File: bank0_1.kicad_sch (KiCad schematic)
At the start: 1 part, among them U1 ECP5-BGA256

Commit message: schematic wip
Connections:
- net +3V3: no longer U1.D10 (PT47A), U1.E10 (PT47B), U1.E11 (PT51B), U1.F10 (VCCIO1_1), U1.F11 (VCCIO1_2)
- net RX_MIX_CTRL.FM: now reaches U1.A2 (PT4A)
- net RX_MIX_CTRL.ENBL: now reaches U1.A3 (PT6A)
- net RX_MIX_CTRL.MODE: now reaches U1.A4 (PT6B)
- net RX_MIX_CTRL.LD: now reaches U1.B3 (PT4B)
- net RX_MIX_CTRL.SCLK: now reaches U1.C4 (PT11A)
- net RX_RCVR.SDA: now reaches U1.C6 (PT22A)
- net ~{RX_MIX_BYPASS}: now reaches U1.C7 (PT27A)
- net RX_MIX_CTRL.~{EN}: now reaches U1.D4 (PT9B)
- net RX_RCVR.GAIN5: now reaches U1.D5 (PT13B)
- net RX_RCVR.GAIN0: now reaches U1.D6 (PT20B)
- net 3V3RX_EN: now reaches U1.D7 (PT24B)
- net RX_MIX_CTRL.~{RESET}: now reaches U1.E4 (PT9A)
- net CLOCK_60MHZ: no longer names the net of U1.A8 (PT29B)
- net LED0: no longer names the net of U1.E13 (PT62B)
- net LED1 renamed AFE_SPI.SCK
- net LED2: no longer names the net of U1.B14 (PT67A)
- net LED3 renamed AFE_ALT_CLK
- net LED4 renamed DA0
- net LED5 renamed DA6
- net MEZZANINE22: no longer names the net of U1.A14 (PT65B)
- net MEZZANINE23 renamed AFE_SPI.PICO
- net MEZZANINE24: no longer names the net of U1.A13 (PT65A)
- net MEZZANINE25 renamed AFE_SPI.~{CS}
- net MEZZANINE26 renamed DA3
- net MEZZANINE27 renamed DA2
- net MEZZANINE28 renamed DA4
- net MEZZANINE3 renamed DD7
- net MEZZANINE4 renamed DD3
- net MEZZANINE5 renamed DD1
- net MEZZANINE6 renamed DD2
- net MEZZANINE7 renamed DA7
- net PMOD_A0 renamed DD5
- net PMOD_A1 renamed DD6
- net PMOD_A2 renamed DA5
- net PMOD_A3 renamed DA1
- net PMOD_A4 renamed DD8
- net PMOD_A5 renamed DD9
- net PMOD_A6 renamed DD4
- net PMOD_A7 renamed DD0
- net PMOD_B0 renamed RX_MIX_CTRL.SDATA
- net PMOD_B1 renamed RX_RCVR.GAIN3
- net PMOD_B2 renamed RX_RCVR.SCL
- net PMOD_B3: no longer names the net of U1.B7 (PT27B)
- net PMOD_B4 renamed RX_RCVR.GAIN4
- net PMOD_B5 renamed RX_RCVR.GAIN2
- net PMOD_B6 renamed RX_RCVR.GAIN1
- net PMOD_B7: no longer names the net of U1.A7 (PT29A)
- new net +1V8: U1.D10 (PT47A), U1.E10 (PT47B), U1.E11 (PT51B), U1.F10 (VCCIO1_1), U1.F11 (VCCIO1_2)
- no-connect marks 12 -> 7
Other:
- moved on the sheet: U1B, U1C

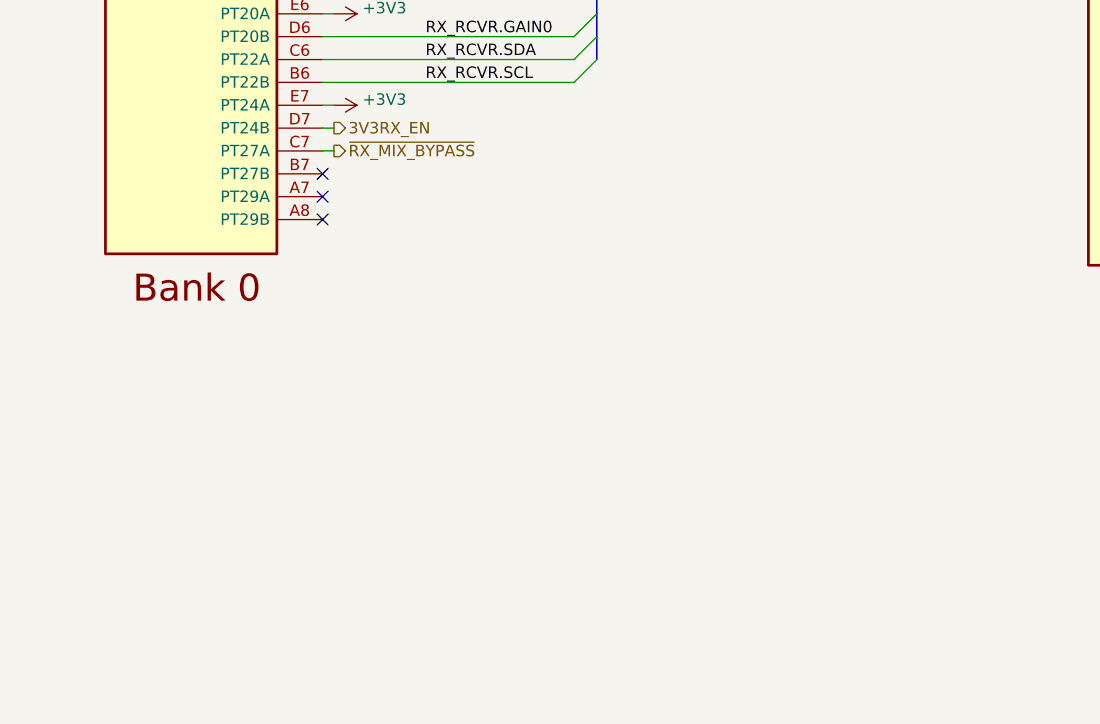
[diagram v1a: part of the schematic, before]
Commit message: add regulator for analog 3.3 V supply
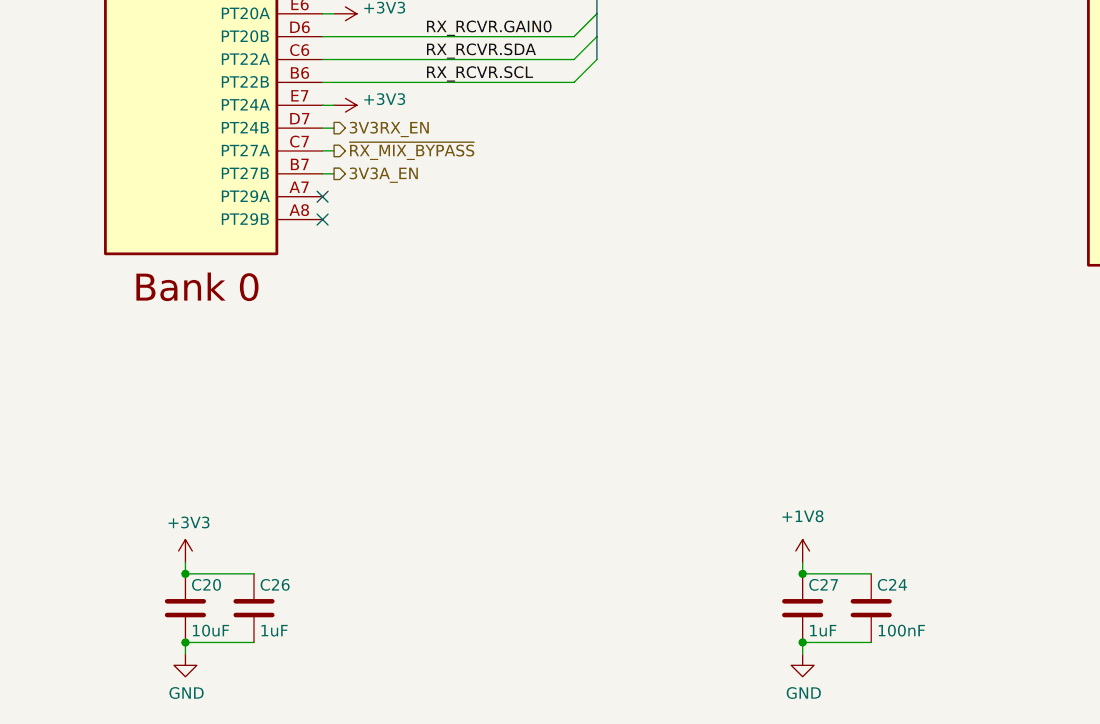
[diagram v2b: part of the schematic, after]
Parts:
- added C20: 10uF, Capacitor_SMD:C_0603_1608Metric, symbol Device:C
- added C24: 100nF, Capacitor_SMD:C_0402_1005Metric, symbol Device:C
- added C26, C27: 1uF, Capacitor_SMD:C_0402_1005Metric, symbol Device:C
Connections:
- net +1V8: now also C24.1, C27.1
- net +3V3: now also C20.1, C26.1
- net GND: now also C20.2, C24.2, C26.2, C27.2
- net 3V3A_EN: now reaches U1.B7 (PT27B)
- no-connect marks 7 -> 6

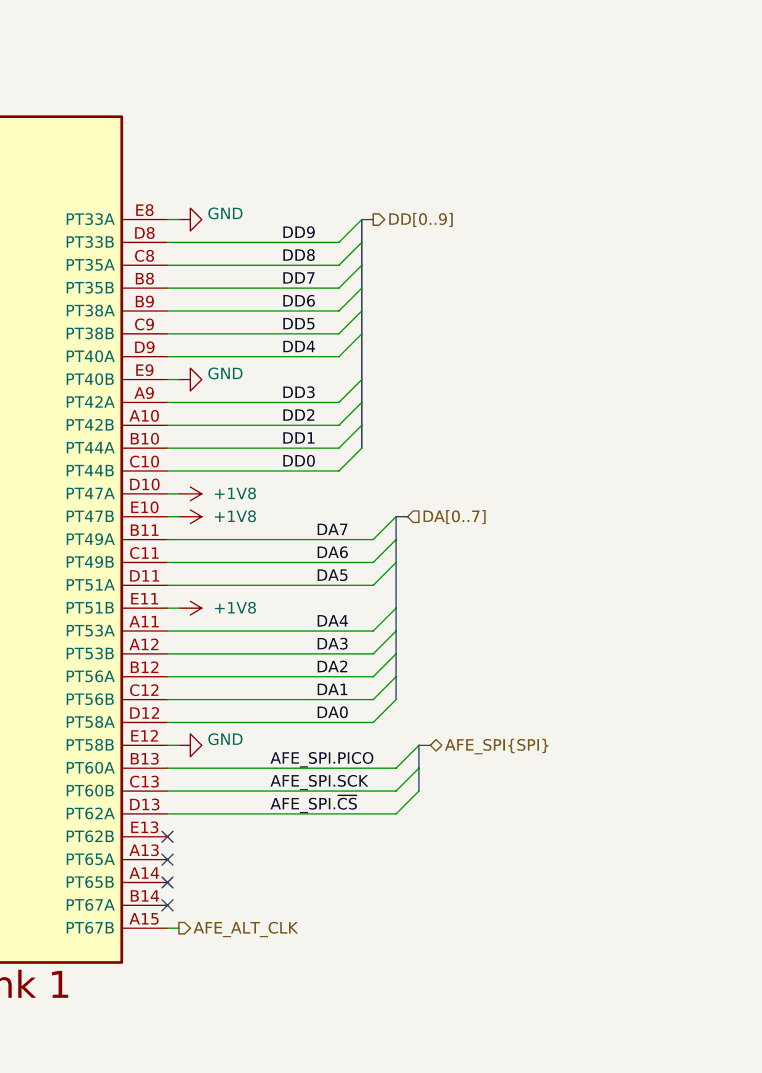
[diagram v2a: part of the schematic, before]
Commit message: ADC/DAC layout
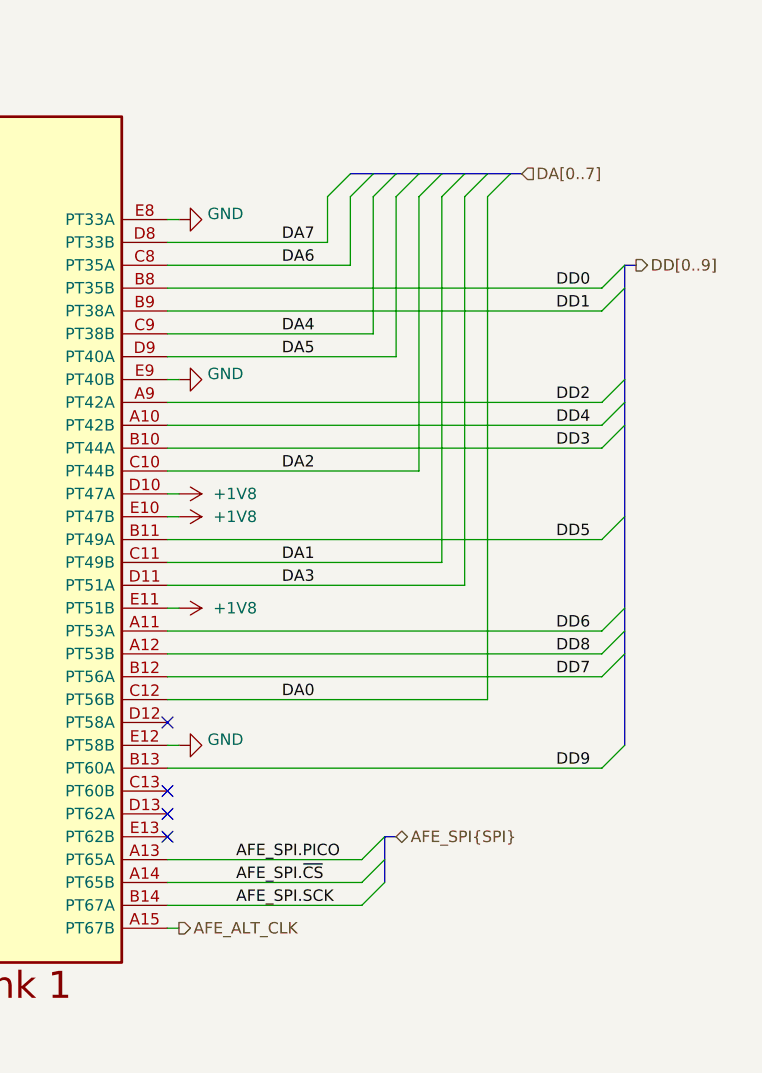
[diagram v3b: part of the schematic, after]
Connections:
- net AFE_SPI.PICO: now also U1.A13 (PT65A); no longer U1.B13 (PT60A)
- net AFE_SPI.SCK: now also U1.B14 (PT67A); no longer U1.C13 (PT60B)
- net AFE_SPI.~{CS}: now also U1.A14 (PT65B); no longer U1.D13 (PT62A)
- net DA0: now also U1.C12 (PT56B); no longer U1.D12 (PT58A)
- net DA1: now also U1.C11 (PT49B); no longer U1.C12 (PT56B)
- net DA2: now also U1.C10 (PT44B); no longer U1.B12 (PT56A)
- net DA3: now also U1.D11 (PT51A); no longer U1.A12 (PT53B)
- net DA4: now also U1.C9 (PT38B); no longer U1.A11 (PT53A)
- net DA5: now also U1.D9 (PT40A); no longer U1.D11 (PT51A)
- net DA6: now also U1.C8 (PT35A); no longer U1.C11 (PT49B)
- net DA7: now also U1.D8 (PT33B); no longer U1.B11 (PT49A)
- net DD0: now also U1.B8 (PT35B); no longer U1.C10 (PT44B)
- net DD1: now also U1.B9 (PT38A); no longer U1.B10 (PT44A)
- net DD2: now also U1.A9 (PT42A); no longer U1.A10 (PT42B)
- net DD3: now also U1.B10 (PT44A); no longer U1.A9 (PT42A)
- net DD4: now also U1.A10 (PT42B); no longer U1.D9 (PT40A)
- net DD5: now also U1.B11 (PT49A); no longer U1.C9 (PT38B)
- net DD6: now also U1.A11 (PT53A); no longer U1.B9 (PT38A)
- net DD7: now also U1.B12 (PT56A); no longer U1.B8 (PT35B)
- net DD8: now also U1.A12 (PT53B); no longer U1.C8 (PT35A)
- net DD9: now also U1.B13 (PT60A); no longer U1.D8 (PT33B)

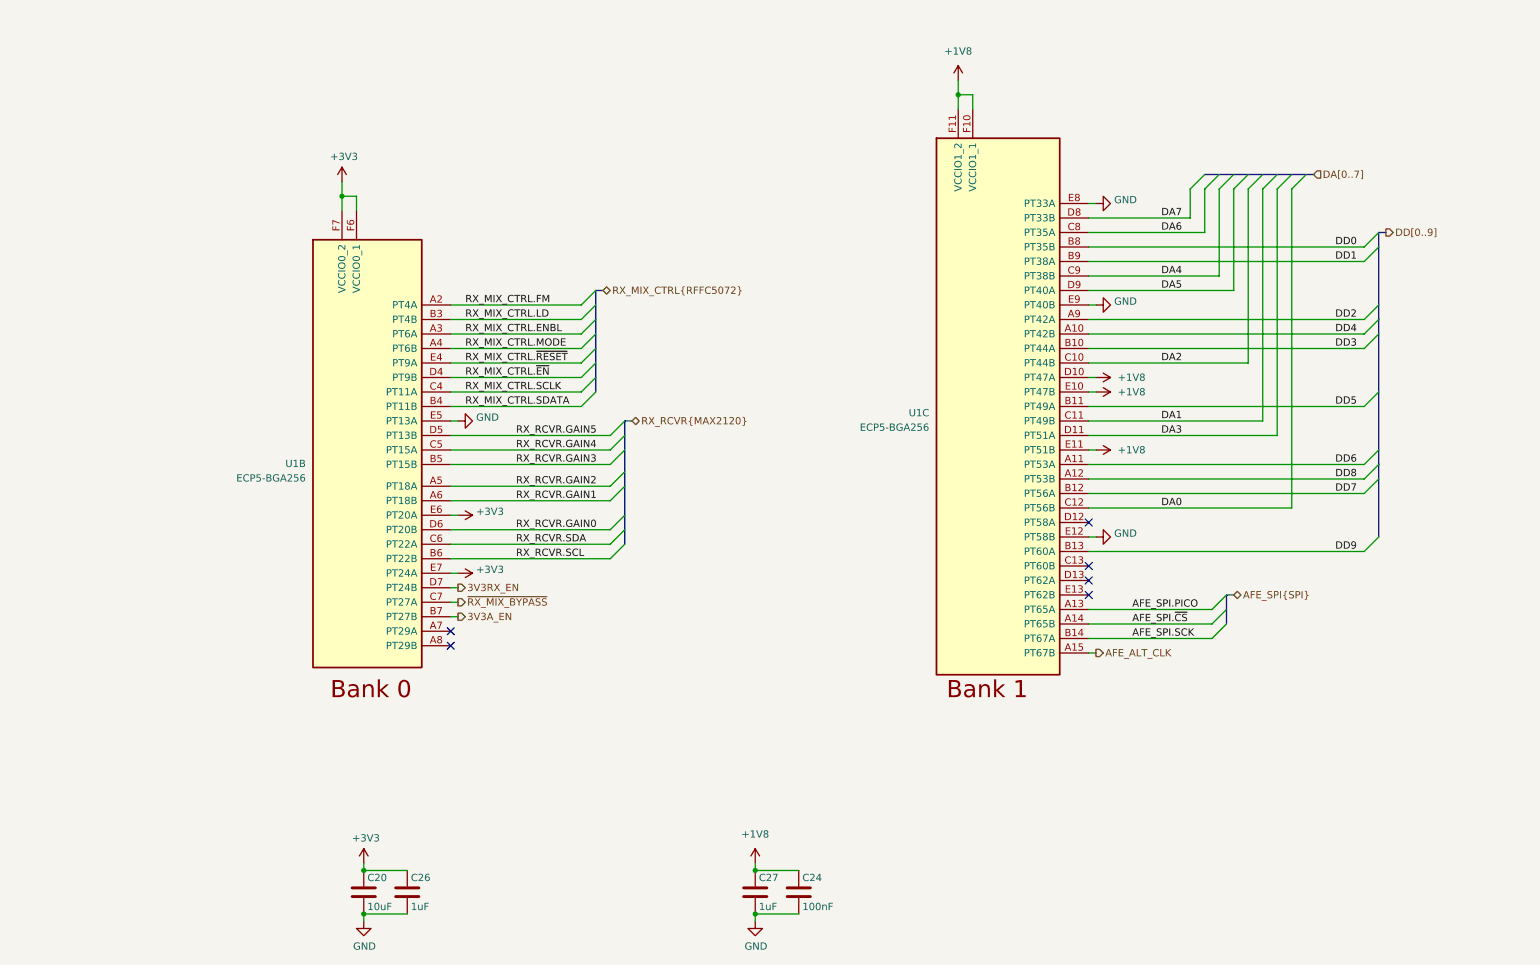
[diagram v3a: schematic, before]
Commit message: layout wip: radio FPGA connections and clocks
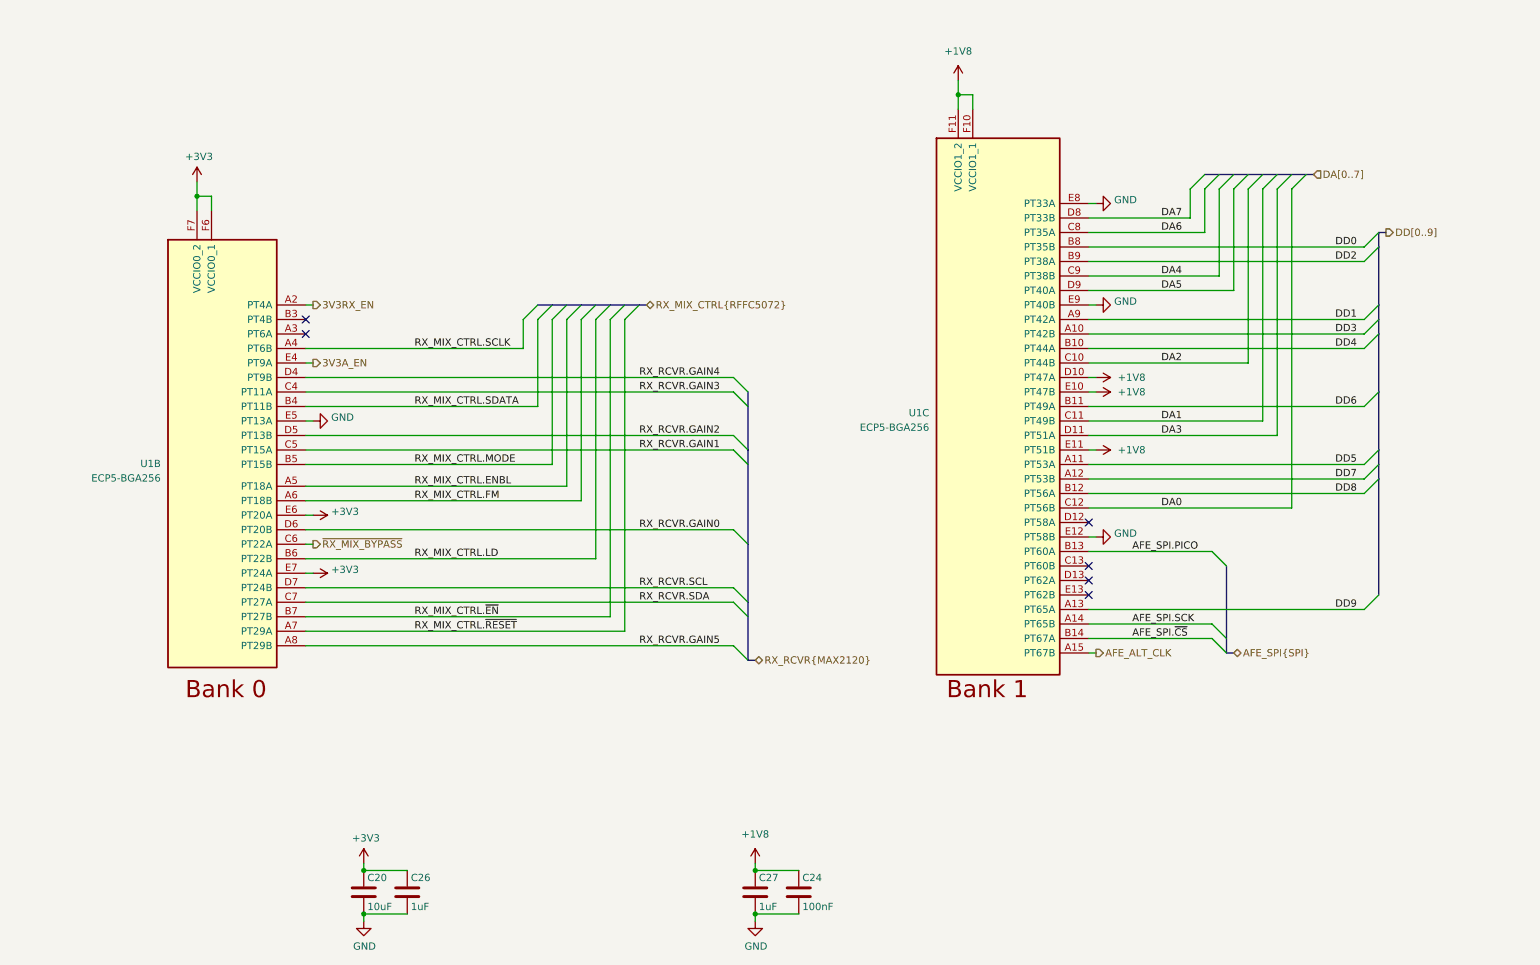
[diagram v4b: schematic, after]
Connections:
- net 3V3A_EN: now also U1.E4 (PT9A); no longer U1.B7 (PT27B)
- net 3V3RX_EN: now also U1.A2 (PT4A); no longer U1.D7 (PT24B)
- net AFE_SPI.PICO: now also U1.B13 (PT60A); no longer U1.A13 (PT65A)
- net AFE_SPI.SCK: now also U1.A14 (PT65B); no longer U1.B14 (PT67A)
- net AFE_SPI.~{CS}: now also U1.B14 (PT67A); no longer U1.A14 (PT65B)
- net DD1: now also U1.A9 (PT42A); no longer U1.B9 (PT38A)
- net DD2: now also U1.B9 (PT38A); no longer U1.A9 (PT42A)
- net DD3: now also U1.A10 (PT42B); no longer U1.B10 (PT44A)
- net DD4: now also U1.B10 (PT44A); no longer U1.A10 (PT42B)
- net DD5: now also U1.A11 (PT53A); no longer U1.B11 (PT49A)
- net DD6: now also U1.B11 (PT49A); no longer U1.A11 (PT53A)
- net DD7: now also U1.A12 (PT53B); no longer U1.B12 (PT56A)
- net DD8: now also U1.B12 (PT56A); no longer U1.A12 (PT53B)
- net DD9: now also U1.A13 (PT65A); no longer U1.B13 (PT60A)
- net RX_MIX_CTRL.ENBL: now also U1.A5 (PT18A); no longer U1.A3 (PT6A)
- net RX_MIX_CTRL.FM: now also U1.A6 (PT18B); no longer U1.A2 (PT4A)
- net RX_MIX_CTRL.LD: now also U1.B6 (PT22B); no longer U1.B3 (PT4B)
- net RX_MIX_CTRL.MODE: now also U1.B5 (PT15B); no longer U1.A4 (PT6B)
- net RX_MIX_CTRL.SCLK: now also U1.A4 (PT6B); no longer U1.C4 (PT11A)
- net RX_MIX_CTRL.~{EN}: now also U1.B7 (PT27B); no longer U1.D4 (PT9B)
- net RX_MIX_CTRL.~{RESET}: now also U1.A7 (PT29A); no longer U1.E4 (PT9A)
- net RX_RCVR.GAIN1: now also U1.C5 (PT15A); no longer U1.A6 (PT18B)
- net RX_RCVR.GAIN2: now also U1.D5 (PT13B); no longer U1.A5 (PT18A)
- net RX_RCVR.GAIN3: now also U1.C4 (PT11A); no longer U1.B5 (PT15B)
- net RX_RCVR.GAIN4: now also U1.D4 (PT9B); no longer U1.C5 (PT15A)
- net RX_RCVR.GAIN5: now also U1.A8 (PT29B); no longer U1.D5 (PT13B)
- net RX_RCVR.SCL: now also U1.D7 (PT24B); no longer U1.B6 (PT22B)
- net RX_RCVR.SDA: now also U1.C7 (PT27A); no longer U1.C6 (PT22A)
- net ~{RX_MIX_BYPASS}: now also U1.C6 (PT22A); no longer U1.C7 (PT27A)
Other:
- moved on the sheet: U1B

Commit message: complete initial layout
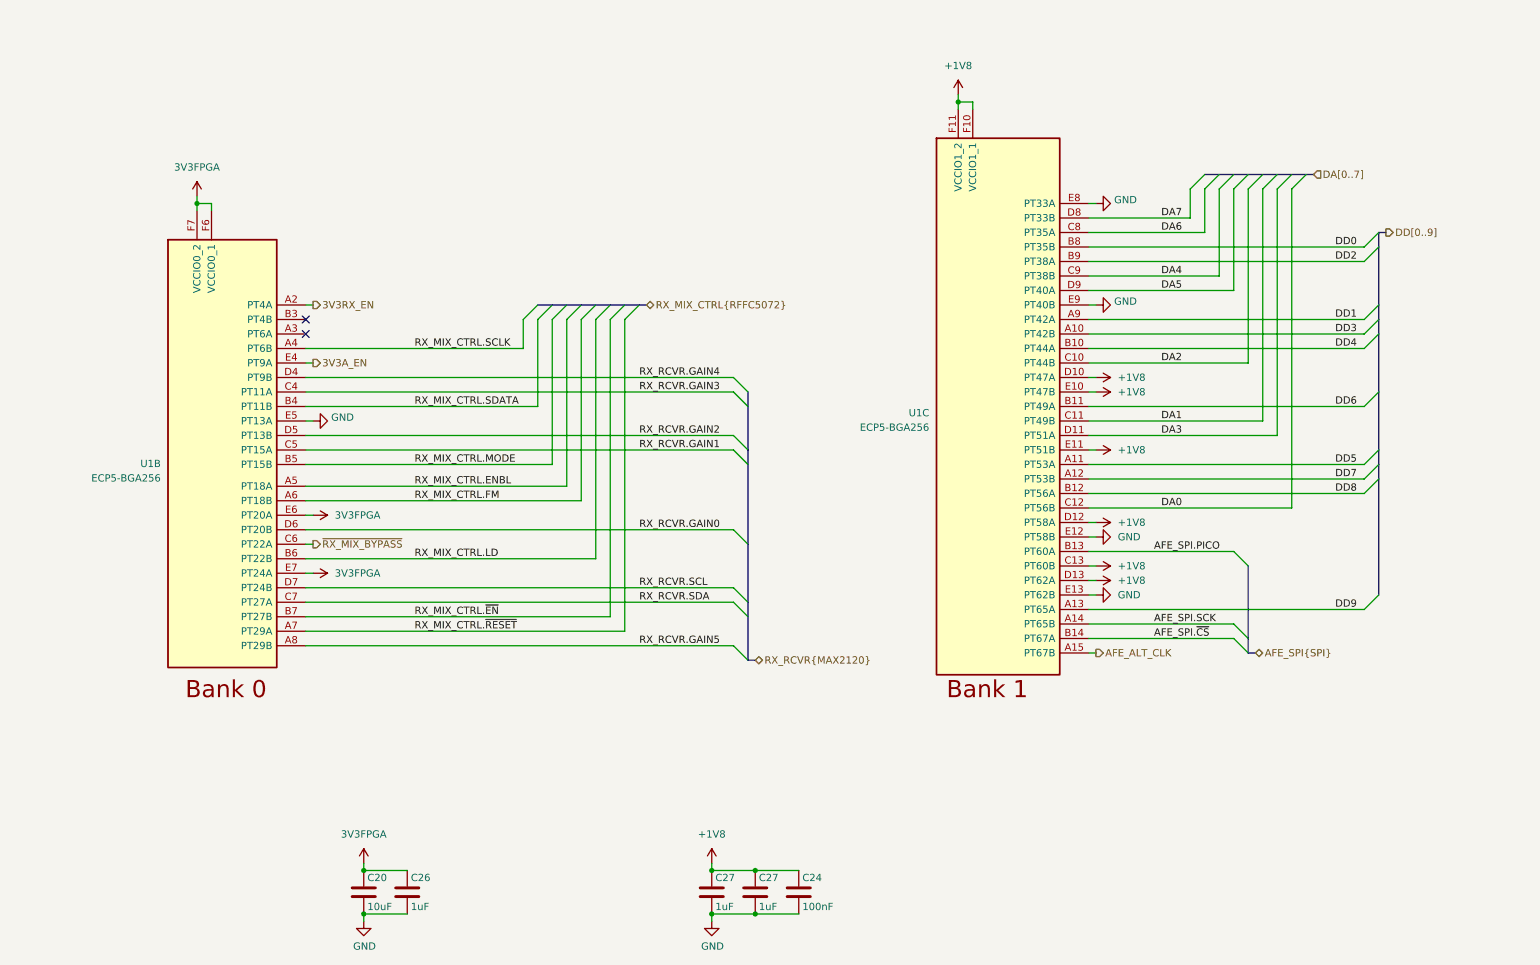
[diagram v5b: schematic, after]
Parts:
- added C27: 1uF, Capacitor_SMD:C_0402_1005Metric, symbol Device:C
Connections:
- net +1V8: now also U1.C13 (PT60B), U1.D12 (PT58A), U1.D13 (PT62A), C27.1
- net GND: now also U1.E13 (PT62B), C27.2
- net +3V3 renamed 3V3FPGA
- no-connect marks 6 -> 2
